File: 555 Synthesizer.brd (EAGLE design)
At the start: 100 x 45.7 mm, 44 parts, among them IC1 555, Q1 FQP27P06, U1 LM7805

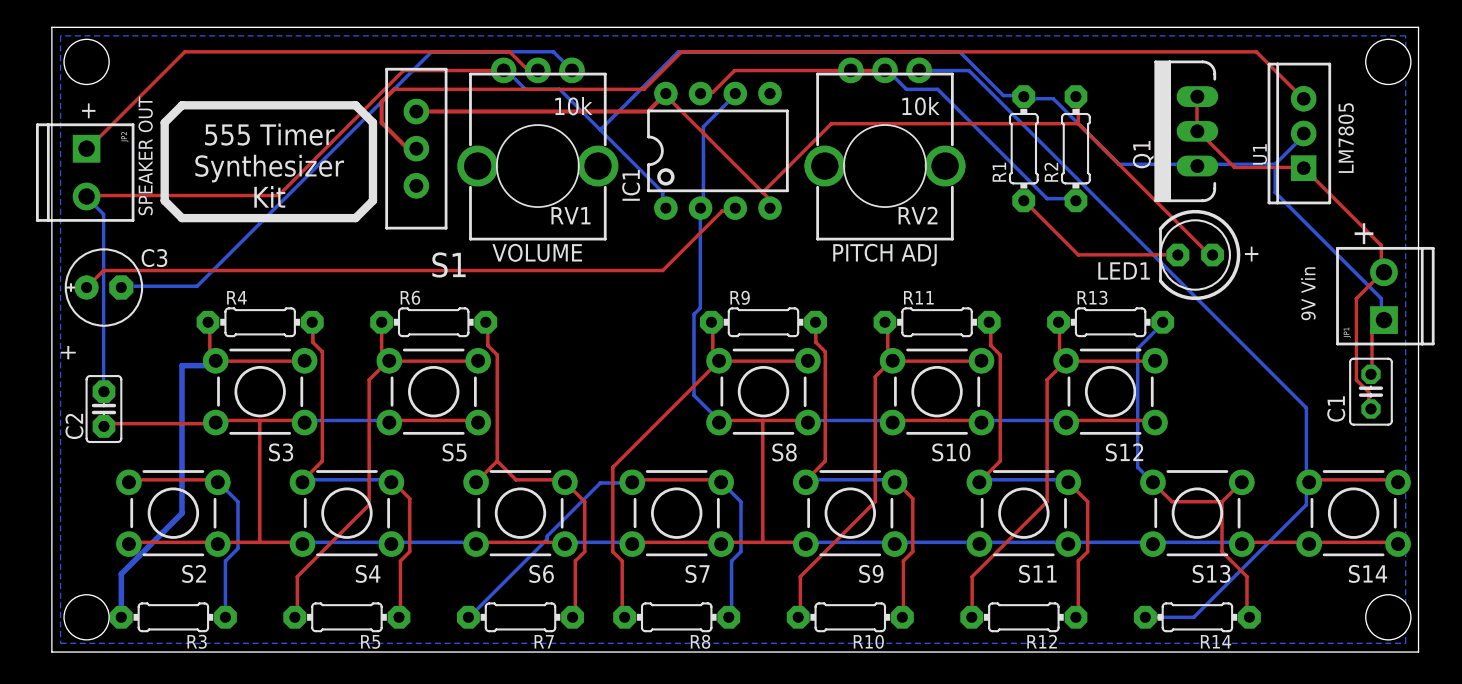
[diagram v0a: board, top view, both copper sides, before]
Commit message: Added CMOS 555
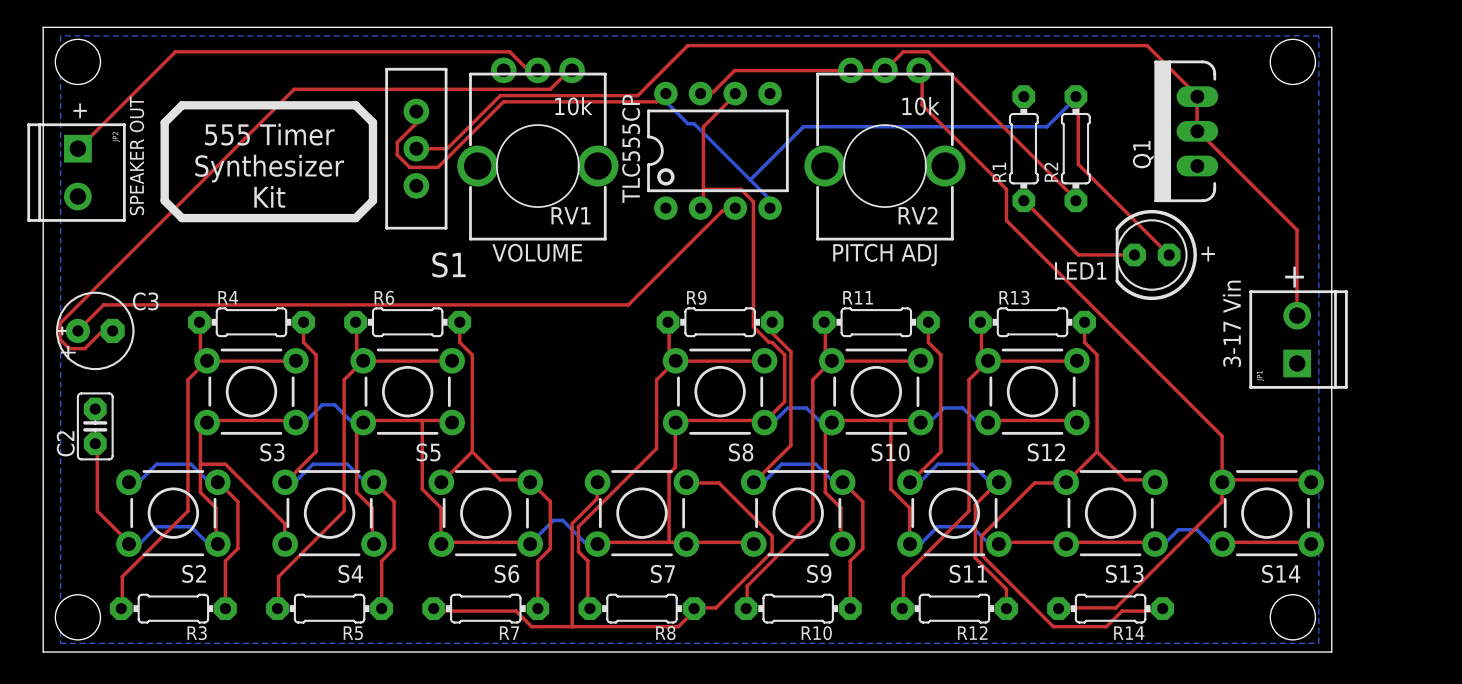
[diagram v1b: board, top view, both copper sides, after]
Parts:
- removed C1: 10uf, adafruit:C025-030X050
- removed U1: LM7805, SparkFun-PowerIC:TO220-IGO
- moved JP1 7.10 mm to (89.9, 18.6)
- moved U$1 6.98 mm to (89.5, 40.6)
- moved U$4 6.98 mm to (89.5, 0.00)
- moved R14 6.38 mm to (76.2, 0.64)
- moved S14 6.35 mm to (87.6, 7.62)
- moved S13 6.35 mm to (76.2, 7.62)
- moved R13 5.72 mm to (70.5, 21.6)
- moved S12 5.72 mm to (70.5, 16.5)
- moved R12 5.12 mm to (64.8, 0.64)
- moved S11 5.08 mm to (64.8, 7.62)
- moved R11 4.45 mm to (59.1, 21.6)
- moved S10 4.45 mm to (59.1, 16.5)
- moved R10 3.86 mm to (53.3, 0.64)
- moved S9 3.81 mm to (53.3, 7.62)
- moved C3 3.24 mm to (1.91, 21.0)
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- renumbered IC1 to TLC555CP
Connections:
- removed net N$3: S1.2, U1.OUT
- net GND: no longer C1.2, U1.GND
- net N$1: now also S1.2; no longer C1.1, U1.IN
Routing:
- net GND: track 143.4 -> 0.00 mm
- net N$3: track 75.3 -> 0.00 mm
- net N$1: track 32.9 -> 80.9 mm
- net TRI: track 199.6 -> 221.2 mm
- net N$14: track 33.8 -> 48.1 mm
- net N$20: track 30.0 -> 43.5 mm
- net N$7: track 40.7 -> 51.0 mm
- net VCC: track 71.4 -> 78.7 mm
- net N$21: track 67.9 -> 62.7 mm
- net N$4: track 12.9 -> 9.73 mm
- net N$10: track 32.4 -> 30.3 mm
- net N$6: track 50.0 -> 51.9 mm
- net N$18: track 30.3 -> 31.6 mm
- net DIS: track 32.1 -> 33.3 mm
- net N$17: track 31.4 -> 30.3 mm
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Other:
- board size 100 x 45.7 mm -> 94.3 x 45.7 mm
- board text added: "3-17 Vin"
- board text removed: "9V Vin"
- board text removed: "LM7805"
- board text removed: "U1"
